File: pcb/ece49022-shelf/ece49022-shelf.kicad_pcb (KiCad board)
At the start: 4 copper layers, 44.2 x 53.6 mm, 69 parts, among them IC1 NAU7802, J1 USB_B_Micro, J2 Conn_01x16_Pin, J3 Conn_01x04_Pin, J4 SM03B-SRSS-TB, J6 Conn_01x02_Pin, J7 Conn_01x02_Pin, SW1 SW_Push, SW2 SW_Push, U2 TPS54202DDCT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

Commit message: more pcb routing
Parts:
- moved SW2 14.1 mm to (157.1, 76.9), turned to 0 degrees
- moved SW1 9.50 mm to (202.1, 74.7)
- moved J1 7.00 mm to (194.9, 80.1)
- moved C8 3.14 mm to (167.4, 105.0)
- moved R6 2.49 mm to (170.2, 105.0)
- moved R7 2.23 mm to (171.2, 106.5), turned to -90 degrees
- moved R11 1.68 mm to (163.7, 69.3), turned to -45 degrees
- moved R10 0.80 mm to (172.1, 103.7), turned to -45 degrees
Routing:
- net +5V: track 39.1 -> 14.0 mm, vias 6 -> 5
- net /RP2350A/~{USB_BOOT}: track 15.7 -> 9.10 mm
- net Net-(U2-EN): track 0.00 -> 5.27 mm, vias 0 -> 2
- net GND: track 33.2 -> 28.0 mm, vias 57 -> 59
- net +12V: track 0.00 -> 2.68 mm
- net /LCD_A: track 6.59 -> 4.65 mm
- net /RP2350A/QSPI_SS: track 16.9 -> 18.0 mm
- net Net-(U2-SW): vias 0 -> 4
- added copper zone on F.Cu, net +12V
- added copper zone on B.Cu, net +5V
- added copper zone on B.Cu, net Net-(U2-SW)

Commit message: working on stuff
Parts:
- added RV1: R_Potentiometer_US, 49022_Footprints:RES_C01R00, F.Cu at (188.0, 88.5)
- R6: value 0 -> 510K
- R7: value 0 -> 105k
- moved J1 0.30 mm to (195.2, 80.1)
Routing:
- net +5V: track 14.0 -> 39.9 mm, vias 5 -> 7
- net /LCD_VO: track 0.00 -> 25.1 mm, vias 0 -> 2
- net /RP2350A/~{USB_BOOT}: track 9.10 -> 0.00 mm
- net GND: track 28.0 -> 28.8 mm, vias 59 -> 60
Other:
- board text added: "Add potentiometer to board"
- board text added: "Verify that the QSPI traces are length matched"
- board text removed: "Look at Layout of Pico 2"

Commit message: more routing
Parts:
- moved SW1 24.4 mm to (182.0, 88.5)
- moved R15 12.7 mm to (158.6, 75.8)
- moved C16 3.42 mm to (188.6, 72.5), turned to 135 degrees
- moved SW2 1.40 mm to (157.1, 78.3)
- moved C29 1.02 mm to (179.6, 78.6)
- moved L2 0.43 mm to (160.8, 100.3)
- moved R16 0.36 mm to (180.2, 85.1)
- moved C21 0.36 mm to (177.9, 85.2)
- moved C18 0.23 mm to (177.2, 82.6)
- moved L3 0.21 mm to (179.8, 82.6)
- moved C19 0.21 mm to (178.3, 82.6)
- moved C10 0.12 mm to (167.3, 96.4)
- moved C11 0.12 mm to (169.4, 96.4)
- moved R10 0.11 mm to (172.2, 103.7), turned to -90 degrees
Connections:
- net Net-(U5-USB_DM) renamed /RP2350A/USB_MCU_D-
- net Net-(U5-USB_DP) renamed /RP2350A/USB_MCU_D+
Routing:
- net +5V: track 39.9 -> 90.2 mm, vias 7 -> 8
- net /RP2350A/~{USB_BOOT}: track 0.00 -> 26.4 mm, vias 0 -> 2
- net /RP2350A/RUN: track 0.00 -> 21.7 mm, vias 0 -> 2
- net /RP2350A/USB_D-: track 0.00 -> 9.20 mm
- net /RP2350A/USB_D+: track 0.00 -> 9.20 mm
- net Net-(R15-Pad1): track 0.00 -> 5.61 mm
- net GND: track 28.8 -> 34.3 mm
- net +3V3: track 19.9 -> 21.7 mm
- net +1V1: track 22.6 -> 23.2 mm
- net /RP2350A/SWCLK: track 11.4 -> 10.9 mm
- net /LCD_VO: track 25.1 -> 25.6 mm
- removed copper zone on B.Cu, net +5V
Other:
- board text added: "Fillet Corners"

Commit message: stuff
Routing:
- net +3V3: track 21.7 -> 20.2 mm
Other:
- board text added: "Fix USB Traces"
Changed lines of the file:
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@@
 		(layer "Edge.Cuts")
 	)
+	(gr_text "Fix USB Traces"
+		(at 150.56 49.51 0)
+		(layer "F.Cu")
+		(effects
+			(font
+				(size 1.5 1.5)
+				(thickness 0.3)
+				(bold yes)
+			)
+			(justify left bottom)
+		)
+	)
 	(gr_text "Add potentiometer to board"
 		(at 151.5872 55.2196 0)
@@
 	)
 	(segment
-		(start 187.989707 74.089707)
-		(end 189.04531 75.14531)
-		(width 0.15)
-		(layer "F.Cu")
-		(net 10)
-	)
-	(segment
 		(start 188.216093 74.089707)
 		(end 188.934411 73.371389)
@@
 		(start 183.090001 79.83)
 		(end 183.360001 80.1)
-		(width 0.2)
+		(width 0.14)
 		(layer "F.Cu")
 		(net 24)
@@
 		(start 182.61 79.83)
 		(end 183.090001 79.83)
-		(width 0.2)
+		(width 0.14)
 		(layer "F.Cu")
 		(net 24)
@@
 		(start 183.360001 80.1)
 		(end 191.7 80.1)
-		(width 0.2)
+		(width 0.14)
 		(layer "F.Cu")
 		(net 24)
@@
 		(start 183.090001 80.82)
 		(end 183.360001 80.55)
-		(width 0.2)
+		(width 0.14)
 		(layer "F.Cu")
 		(net 25)
@@
 		(start 183.360001 80.55)
 		(end 191.7 80.55)
-		(width 0.2)
+		(width 0.14)
 		(layer "F.Cu")
 		(net 25)
@@
 		(start 182.61 80.82)
 		(end 183.090001 80.82)
-		(width 0.2)
+		(width 0.14)
 		(layer "F.Cu")
 		(net 25)
@@
 		(start 176.771803 80.749999)
 		(end 177.421802 80.1)
-		(width 0.2)
+		(width 0.14)
 		(layer "F.Cu")
 		(net 51)
@@
 		(start 176.0375 80.775)
 		(end 176.062501 80.749999)
-		(width 0.2)
+		(width 0.14)
 		(layer "F.Cu")
 		(net 51)
@@
 		(start 180.839999 80.1)
 		(end 181.109999 79.83)
-		(width 0.2)
+		(width 0.14)
 		(layer "F.Cu")
 		(net 51)
@@
 		(start 176.062501 80.749999)
 		(end 176.771803 80.749999)
-		(width 0.2)
+		(width 0.14)
 		(layer "F.Cu")
 		(net 51)
@@
 		(start 177.421802 80.1)
 		(end 180.839999 80.1)
-		(width 0.2)
+		(width 0.14)
 		(layer "F.Cu")
 		(net 51)
@@
 		(start 181.109999 79.83)
 		(end 181.59 79.83)
-		(width 0.2)
+		(width 0.14)
 		(layer "F.Cu")
 		(net 51)
@@
 		(start 176.958197 81.200001)
 		(end 177.608198 80.55)
-		(width 0.2)
+		(width 0.14)
 		(layer "F.Cu")
 		(net 52)
@@
 		(start 176.0375 81.175)
 		(end 176.062501 81.200001)
-		(width 0.2)
+		(width 0.14)
 		(layer "F.Cu")
 		(net 52)
@@
 		(start 180.839999 80.55)
 		(end 181.109999 80.82)
-		(width 0.2)
+		(width 0.14)
 		(layer "F.Cu")
 		(net 52)
@@
 		(start 181.109999 80.82)
 		(end 181.59 80.82)
-		(width 0.2)
+		(width 0.14)
 		(layer "F.Cu")
 		(net 52)
@@
 		(start 176.062501 81.200001)
 		(end 176.958197 81.200001)
-		(width 0.2)
+		(width 0.14)
 		(layer "F.Cu")
 		(net 52)
@@
 		(start 177.608198 80.55)
 		(end 180.839999 80.55)
-		(width 0.2)
+		(width 0.14)
 		(layer "F.Cu")
 		(net 52)
@@
 		(polygon
 			(pts
-				(xy 167.0304 100.2792) (xy 167.0304 102.3112) (xy 165.0492 102.3112) (xy 165.0492 103.1748) (xy 168.5036 103.1748)
-				(xy 168.6052 103.1748) (xy 168.6052 100.2792)
+				(xy 167.0304 100.2792) (xy 167.0304 102.3112) (xy 165.0492 102.3112) (xy 165.0492 103.8648) (xy 168.6052 103.8648)
+				(xy 168.6052 100.2792)
 			)
 		)

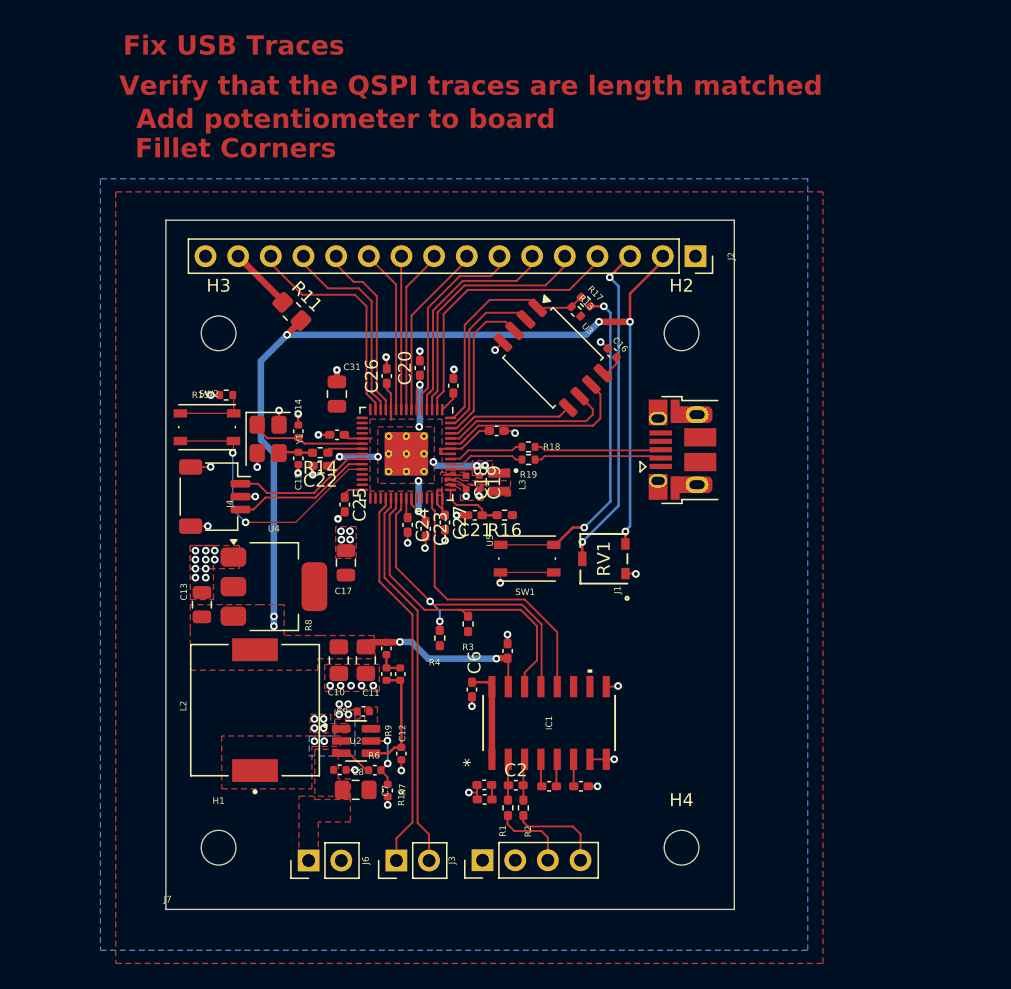
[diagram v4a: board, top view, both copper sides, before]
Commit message: new converter layout
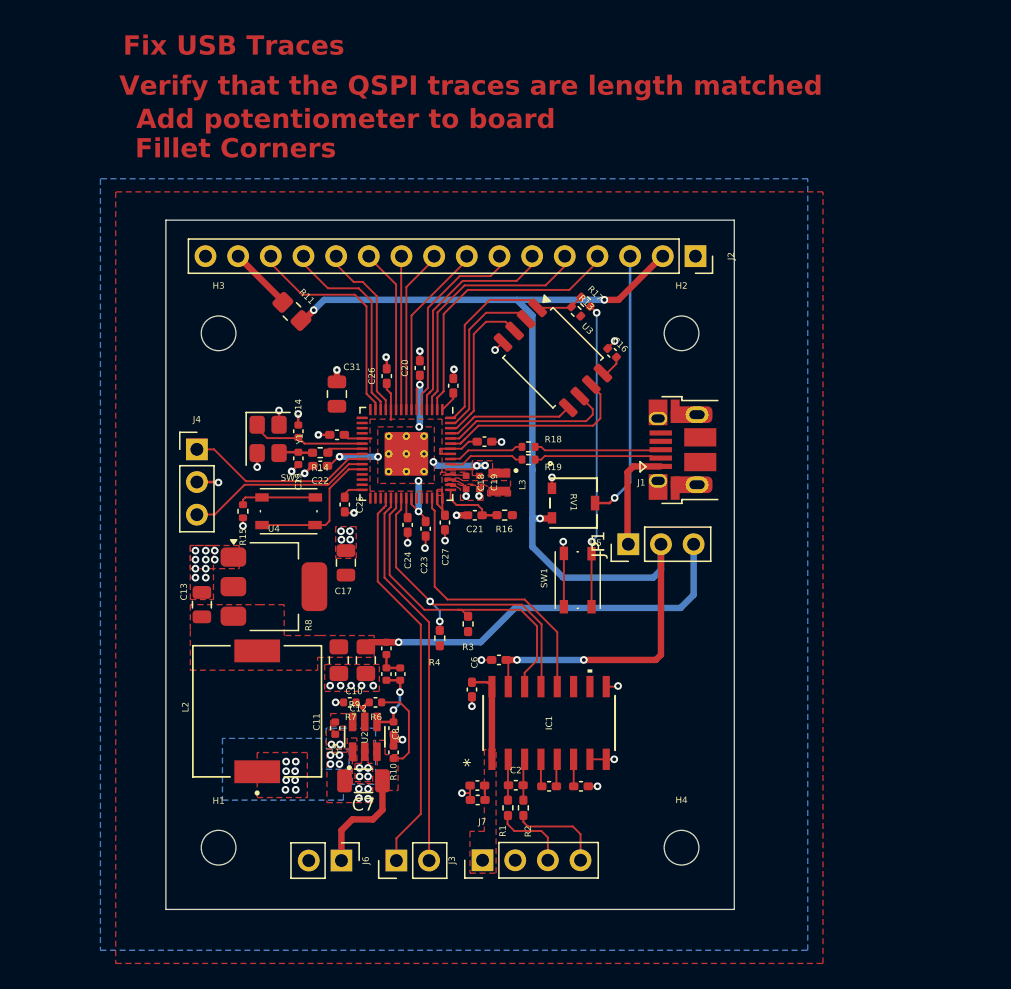
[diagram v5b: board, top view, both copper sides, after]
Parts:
- added JP1: Jumper_3_Bridged12, Connector_PinHeader_2.54mm:PinHeader_1x03_P2.54mm_Vertical, F.Cu at (189.9, 87.4)
- C7: footprint Capacitor_SMD:C_0805_2012Metric_Pad1.18x1.45mm_HandSolder -> Capacitor_SMD:C_1206_3216Metric
- J4: value SM03B-SRSS-TB -> Conn_01x03_Pin; footprint Connector_JST:JST_SH_SM03B-SRSS-TB_1x03-1MP_P1.00mm_Horizontal -> Connector_PinHeader_2.54mm:PinHeader_1x03_P2.54mm_Vertical
- moved R15 9.13 mm to (159.9, 84.8), turned to -90 degrees
- moved SW2 9.11 mm to (163.4, 84.8)
- moved R7 7.46 mm to (168.2, 99.7), turned to 180 degrees
- moved R6 5.28 mm to (170.2, 99.7), turned to 180 degrees
- moved RV1 4.93 mm to (185.6, 84.2), turned to -90 degrees
- moved C8 4.40 mm to (171.6, 103.6), turned to 90 degrees
- moved SW1 4.27 mm to (185.9, 90.2), turned to 90 degrees
- moved J4 3.93 mm to (156.3, 80.0), turned to 0 degrees
- moved J7 2.55 mm to (167.6, 112.0), turned to -90 degrees
- moved C9 2.54 mm to (167.1, 101.7), turned to 90 degrees
- moved R10 2.07 mm to (171.6, 101.7)
- moved C29 1.26 mm to (178.7, 79.4)
- moved C32 0.97 mm to (179.8, 96.4), turned to 180 degrees
- moved C7 0.92 mm to (169.3, 105.8), turned to 180 degrees
- moved U2 0.75 mm to (169.4, 102.4), turned to 90 degrees
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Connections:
- net /RP2350A/USB_MCU_D+ renamed Net-(U5-USB_DP)
- net /RP2350A/USB_MCU_D- renamed Net-(U5-USB_DM)
- C10 pad 1: +5V -> /Power/5V_SREG
- C11 pad 1: +5V -> /Power/5V_SREG
- C13 pad 1: +5V -> /Power/5V_SREG
- J1 pad 1: /RP2350A/5V_USB -> /5V_USB
- L2 pad 2: +5V -> /Power/5V_SREG
- R8 pad 1: +5V -> /Power/5V_SREG
- U4 pad 3: +5V -> /Power/5V_SREG
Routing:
- net /Power/5V_SREG: track 0.00 -> 31.1 mm, vias 0 -> 1
- net +12V: track 2.68 -> 15.5 mm
- net /RP2350A/RUN: track 21.7 -> 11.1 mm, vias 2 -> 0
- net /5V_USB: track 0.00 -> 8.39 mm
- net /LCD_VO: track 25.6 -> 21.0 mm, vias 2 -> 1
- net /RP2350A/SWCLK: track 10.9 -> 14.6 mm
- net /RP2350A/SWD: track 10.9 -> 14.5 mm
- net /Power/FB: track 8.88 -> 5.82 mm, vias 0 -> 2
- net /RP2350A/~{USB_BOOT}: track 26.4 -> 23.9 mm
- net Net-(U2-EN): track 5.27 -> 2.84 mm, vias 2 -> 0
- net +5V: track 90.2 -> 88.1 mm, vias 8 -> 5
- net GND: track 34.3 -> 32.5 mm, vias 60 -> 63
- net +3V3: track 20.2 -> 18.9 mm
- net /MAIN_MCU_I2C_SDA: track 30.0 -> 30.6 mm
- net Net-(U2-SW): vias 4 -> 10
- added copper zone on F.Cu, net /Power/5V_SREG
- added copper zone on F.Cu, net AVDD
- removed copper zone on F.Cu, net +5V

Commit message: stuff
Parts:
- added J5: Conn_02x03_Counter_Clockwise, Connector_PinHeader_2.54mm:PinHeader_2x03_P2.54mm_Vertical, F.Cu at (190.4, 98.8)
- moved C6 1.66 mm to (176.6, 97.5), turned to 90 degrees
- moved R15 1.42 mm to (158.7, 85.6), turned to 90 degrees
- moved SW2 1.26 mm to (162.2, 85.0), turned to 180 degrees
- moved C2 1.20 mm to (179.9, 106.1)
- moved C32 1.20 mm to (178.6, 96.4)
- moved C5 1.20 mm to (185.0, 106.2)
- moved C1 1.20 mm to (182.5, 106.2)
- moved IC1 1.20 mm to (182.5, 101.3)
- moved R1 1.20 mm to (179.3, 107.9)
- moved R2 1.20 mm to (180.5, 107.9)
- moved C4 0.72 mm to (177.4, 106.1)
- moved C3 0.72 mm to (177.4, 107.2)
- moved C25 0.59 mm to (167.9, 84.9)
- moved R3 0.10 mm to (177.4, 93.5)
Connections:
- U5 pad 27: /RP2350A/GPIO16 -> /GPIO_AUX_16
- U5 pad 28: /RP2350A/GPIO17 -> /GPIO_AUX_17
- U5 pad 29: /RP2350A/GPIO18 -> /GPIO_AUX_18
- U5 pad 31: /RP2350A/GPIO19 -> /GPIO_AUX_19
- U5 pad 32: /RP2350A/GPIO20 -> /GPIO_AUX_20
- U5 pad 33: /RP2350A/GPIO21 -> /GPIO_AUX_21
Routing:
- net /GPIO_AUX_21: track 0.00 -> 48.4 mm, vias 0 -> 1
- net /GPIO_AUX_20: track 0.00 -> 45.6 mm, vias 0 -> 1
- net /GPIO_AUX_16: track 0.00 -> 44.4 mm, vias 0 -> 1
- net /GPIO_AUX_19: track 0.00 -> 42.9 mm, vias 0 -> 1
- net /GPIO_AUX_17: track 0.00 -> 41.1 mm, vias 0 -> 1
- net /GPIO_AUX_18: track 0.00 -> 38.7 mm, vias 0 -> 1
- net GND: track 32.5 -> 36.3 mm, vias 63 -> 78
- net +5V: track 88.1 -> 85.6 mm
- net /LOAD_CELL_I2C_SDA: track 25.8 -> 24.0 mm
- net /Power/5V_SREG: track 31.1 -> 32.5 mm
- net /RP2350A/RUN: track 11.1 -> 9.99 mm
- net /LOAD_CELL_P: track 6.02 -> 6.81 mm
- net /MAIN_MCU_I2C_SDA: track 30.6 -> 30.1 mm
- net +3V3: track 18.9 -> 19.2 mm, vias 0 -> 6
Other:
- board text added: "Labels for Jumpers LED Fix USB Traces QSPI Length Match Round Corners on Pokygons"
- board text removed: "Add potentiometer to board"
- board text removed: "Fillet Corners"
- board text removed: "Fix USB Traces"
- board text removed: "Verify that the QSPI traces are length matched"

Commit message: layout chanes
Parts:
- moved R19 1.25 mm to (180.8, 80.8)
- moved R18 1.25 mm to (180.8, 79.8)
- moved C31 0.78 mm to (167.2, 76.5)
- moved H1 0.60 mm to (158.0, 111.6)
- moved H4 0.60 mm to (194.0, 111.6)
- moved R3 0.25 mm to (177.4, 93.2)
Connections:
- net Net-(U5-USB_DM) renamed /RP2350A/USB_DN
- net Net-(U5-USB_DP) renamed /RP2350A/USB_DP
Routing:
- net +3V3: track 19.2 -> 23.1 mm, vias 6 -> 0
- net +5V: track 85.6 -> 88.3 mm
- net /RP2350A/USB_D-: track 9.20 -> 11.2 mm
- net /RP2350A/USB_D+: track 9.20 -> 11.1 mm
- net /GPIO_AUX_18: track 38.7 -> 37.1 mm
- net /RP2350A/USB_DN: track 5.94 -> 4.60 mm
- net /Power/5V_SREG: track 32.5 -> 31.2 mm
- net /RP2350A/USB_DP: track 5.94 -> 4.71 mm
- net /GPIO_AUX_16: track 44.4 -> 43.4 mm
- net /GPIO_AUX_19: track 42.9 -> 42.0 mm
- net /GPIO_AUX_17: track 41.1 -> 40.2 mm
- net /LOAD_CELL_DRDY: track 22.7 -> 22.1 mm
- net /LCD_RS/DI: track 21.7 -> 21.1 mm
- net /LCD_R_W: track 19.9 -> 19.4 mm
- net GND: track 36.3 -> 36.8 mm, vias 78 -> 139
- added copper zone on B.Cu, net GND
- removed copper zone on B.Cu, net +3V3
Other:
- board text added: "Labels for Jumpers LED Fix USB Traces QSPI Length Match Round Corners on Pokygons LED Pin + Resistor"
- board text removed: "Labels for Jumpers LED Fix USB Traces QSPI Length Match Round Corners on Pokygons"

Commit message: stuff
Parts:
- added D1: LED, Resistor_SMD:R_0603_1608Metric, F.Cu at (169.3, 92.2)
- added D2: D_Schottky, 49022_Footprints:SMFDO-219AB_VIS-L, F.Cu at (168.1, 108.9)
- added J8: Conn_02x03_Counter_Clockwise, Connector_PinHeader_2.54mm:PinHeader_2x03_P2.54mm_Vertical, F.Cu at (190.1, 106.3)
- added R12: 100, Resistor_SMD:R_0603_1608Metric, F.Cu at (167.7, 92.2)
- added R20: 100, Resistor_SMD:R_0603_1608Metric, F.Cu at (193.2, 94.2)
- J6: value Conn_01x02_Pin -> Conn_01x03_Pin; footprint Connector_PinHeader_2.54mm:PinHeader_1x02_P2.54mm_Vertical -> Connector_PinHeader_2.54mm:PinHeader_1x03_P2.54mm_Vertical
- moved J6 1.62 mm to (170.2, 112.0)
- moved J7 1.28 mm to (166.3, 112.0)
- moved J3 1.00 mm to (179.5, 112.0)
- moved J5 0.82 mm to (190.1, 99.5), turned to 90 degrees
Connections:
- J5 pad 6: /GPIO_AUX_21 -> /LED
- J7 pad 1: +12V -> Net-(D2-A)
- U5 pad 33: /GPIO_AUX_21 -> /RP2350A/GPIO21
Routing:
- net /GPIO_AUX_21: track 48.6 -> 0.00 mm, vias 1 -> 0
- net /RP2350A/GPIO21: track 0.00 -> 31.9 mm, vias 0 -> 2
- net /GPIO_AUX_20: track 45.3 -> 34.3 mm
- net /GPIO_AUX_19: track 42.0 -> 32.5 mm
- net +12V: track 15.5 -> 10.4 mm
- net /GPIO_AUX_16: track 43.4 -> 48.0 mm
- net GND: track 36.8 -> 41.3 mm, vias 139 -> 131
- net /LED: track 0.00 -> 3.62 mm
- net Net-(D2-A): track 0.00 -> 3.20 mm
- net /GPIO_AUX_17: track 40.2 -> 42.7 mm
- net Net-(D1-A): track 0.00 -> 1.60 mm
- net /MAIN_MCU_I2C_SDA: track 30.1 -> 30.8 mm
- net /LOAD_CELL_N: track 7.43 -> 8.09 mm
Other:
- board text added: "+12V"
- board text added: "16"
- board text added: "17"
- board text added: "18"
- board text added: "19"
- board text added: "20"
- board text added: "21"
- board text added: "5V_SREG"
- board text added: "5V_USB"
- board text added: "AVDD"
- board text added: "GND"
- board text added: "SCL"
- board text added: "SDA"
- board text added: "SWCLK"
- board text added: "SWD"
- board text removed: "Labels for Jumpers LED Fix USB Traces QSPI Length Match Round Corners on Pokygons LED Pin + Resistor"
